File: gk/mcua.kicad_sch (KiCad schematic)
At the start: 16 parts, among them SW1 SW_Push, SW2 SW_Push, U4 STM32H747BITx, Y1 16MHz

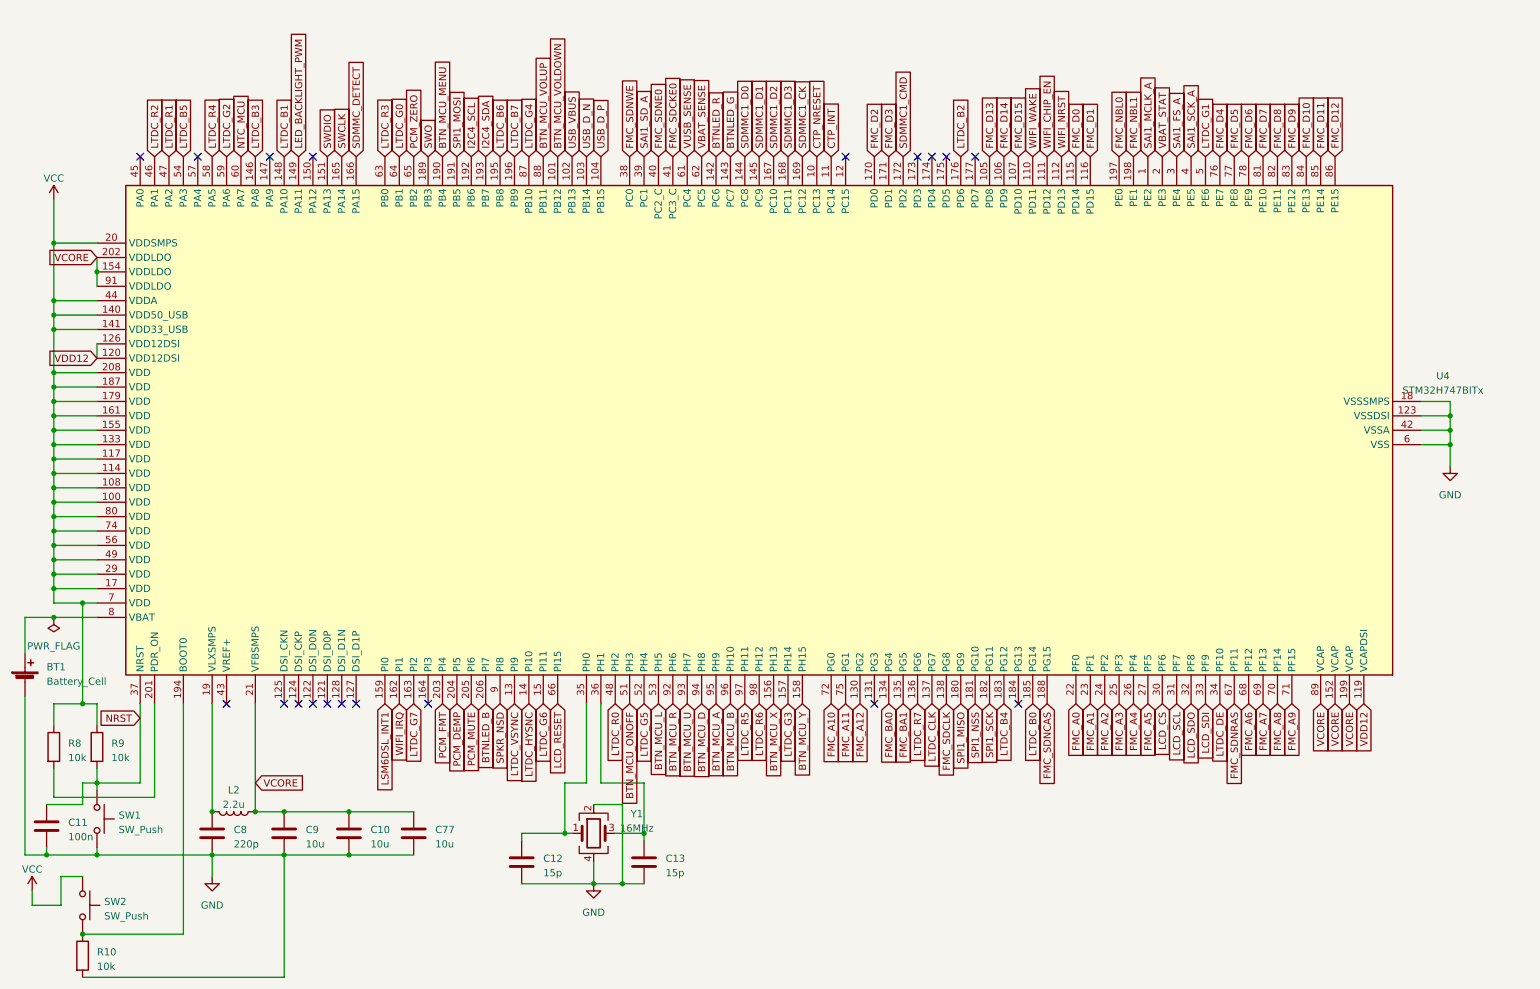
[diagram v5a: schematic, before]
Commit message: Flip lcd sockets to back
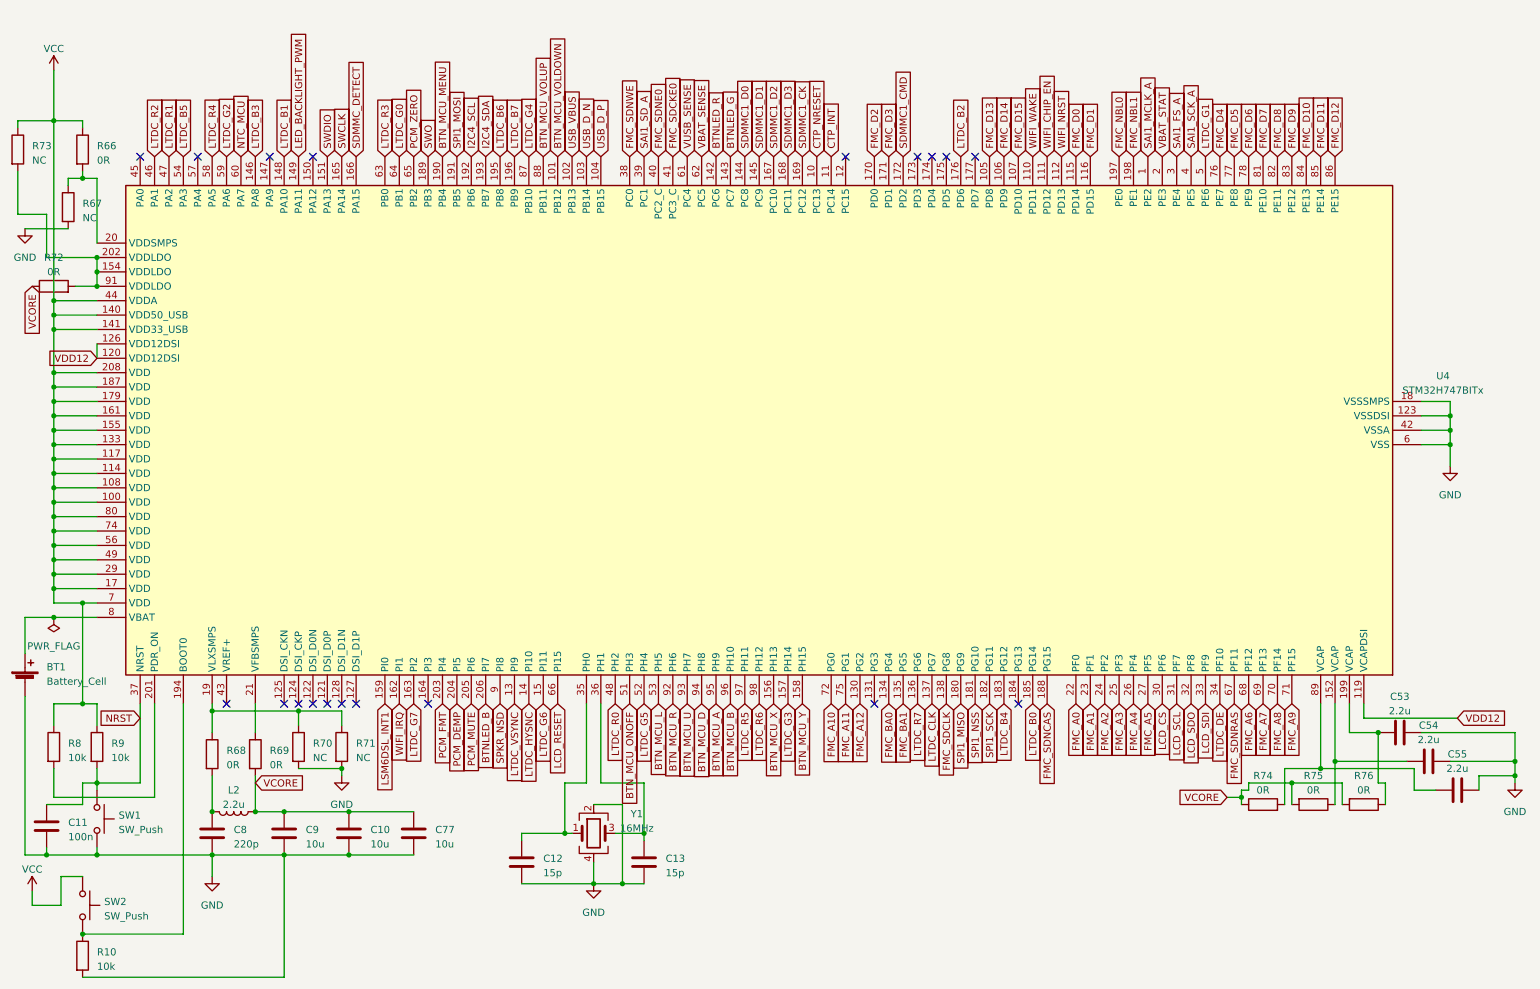
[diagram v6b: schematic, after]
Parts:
- added C53, C54, C55: 2.2u, Capacitor_SMD:C_0805_2012Metric, symbol Device:C
- added R66, R68, R69, R72, R74, R75, R76: 0R, Resistor_SMD:R_0603_1608Metric, symbol Device:R
- added R67, R70, R71, R73: NC, Resistor_SMD:R_0603_1608Metric, symbol Device:R
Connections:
- net GND: now also C53.2, C54.2, C55.2, R67.2, R70.2, R71.2
- net VCC: now also R66.1, R73.1; no longer U4.20 (VDDSMPS)
- net VCORE: now also R69.2, R72.1, R74.1, R75.2, R76.2; no longer U4.152 (VCAP), U4.154 (VDDLDO), U4.199 (VCAP), U4.202 (VDDLDO), U4.21 (VFBSMPS), U4.89 (VCAP), U4.91 (VDDLDO)
- net at C8.1, L2.2: now also R68.2; no longer U4.19 (VLXSMPS)
- new net: C53.1, R76.1, U4.199 (VCAP)
- new net: R68.1, R70.1, R71.1, U4.19 (VLXSMPS)
- new net: C54.1, R75.1, U4.152 (VCAP)
- new net: R72.2, R73.2, U4.154 (VDDLDO), U4.202 (VDDLDO), U4.91 (VDDLDO)
- new net: R69.1, U4.21 (VFBSMPS)
- new net: C55.1, R74.2, U4.89 (VCAP)
- new net: R66.2, R67.1, U4.20 (VDDSMPS)

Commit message: remove unnecessary components
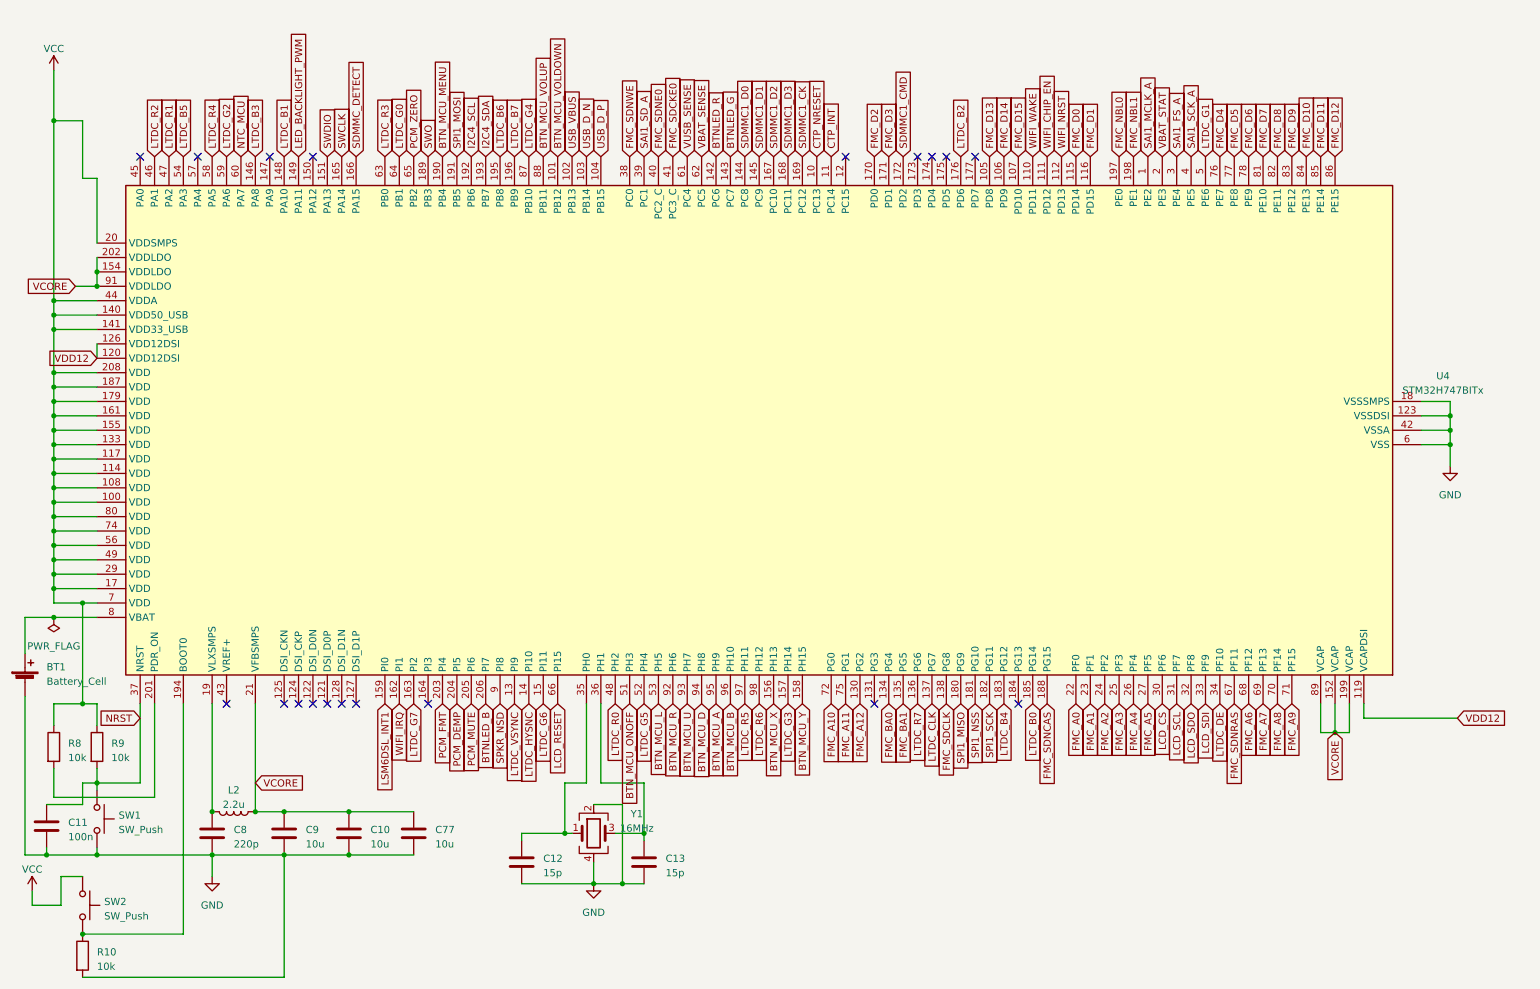
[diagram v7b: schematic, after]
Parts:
- removed C53, C54, C55: 2.2u, Capacitor_SMD:C_0805_2012Metric, symbol Device:C
- removed R66, R68, R69, R72, R74, R75, R76: 0R, Resistor_SMD:R_0603_1608Metric, symbol Device:R
- removed R67, R70, R71, R73: NC, Resistor_SMD:R_0603_1608Metric, symbol Device:R
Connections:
- net VCC: now also U4.20 (VDDSMPS)
- net VCORE: now also U4.152 (VCAP), U4.154 (VDDLDO), U4.199 (VCAP), U4.202 (VDDLDO), U4.21 (VFBSMPS), U4.89 (VCAP), U4.91 (VDDLDO)
- net at C8.1, L2.2: now also U4.19 (VLXSMPS)
